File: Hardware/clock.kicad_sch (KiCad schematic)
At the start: 7 parts, among them U6 SI53365, X1 ASV-24.576MHz-EJ-T

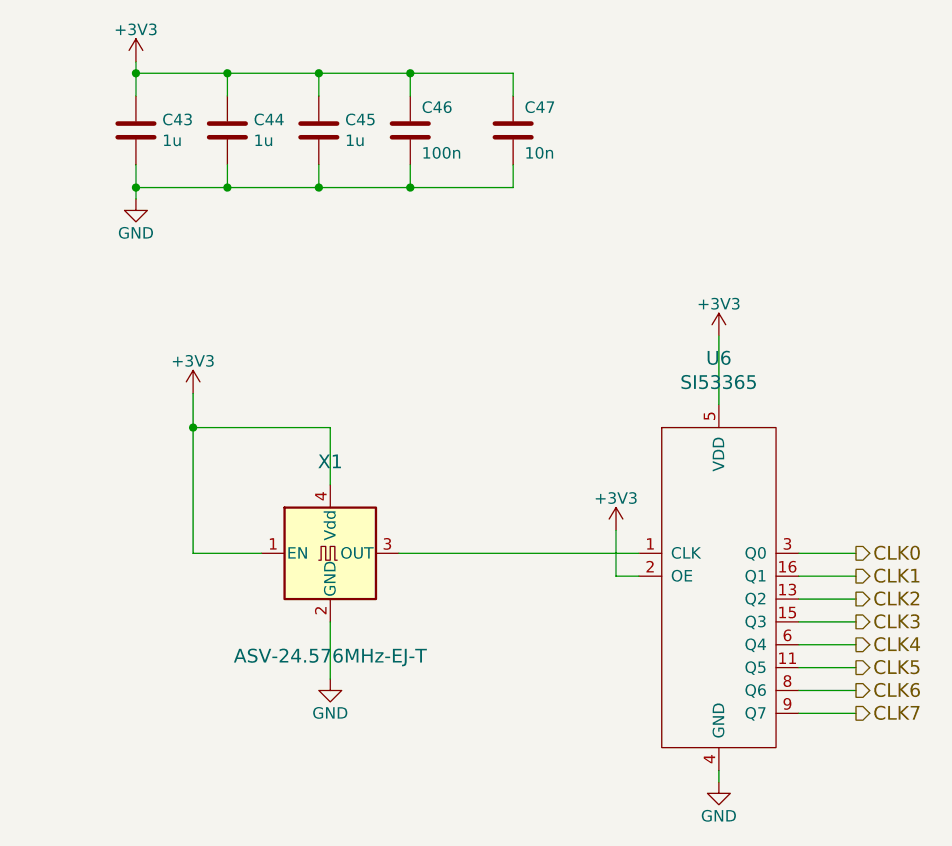
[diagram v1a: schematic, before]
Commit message: Updated clock buffer
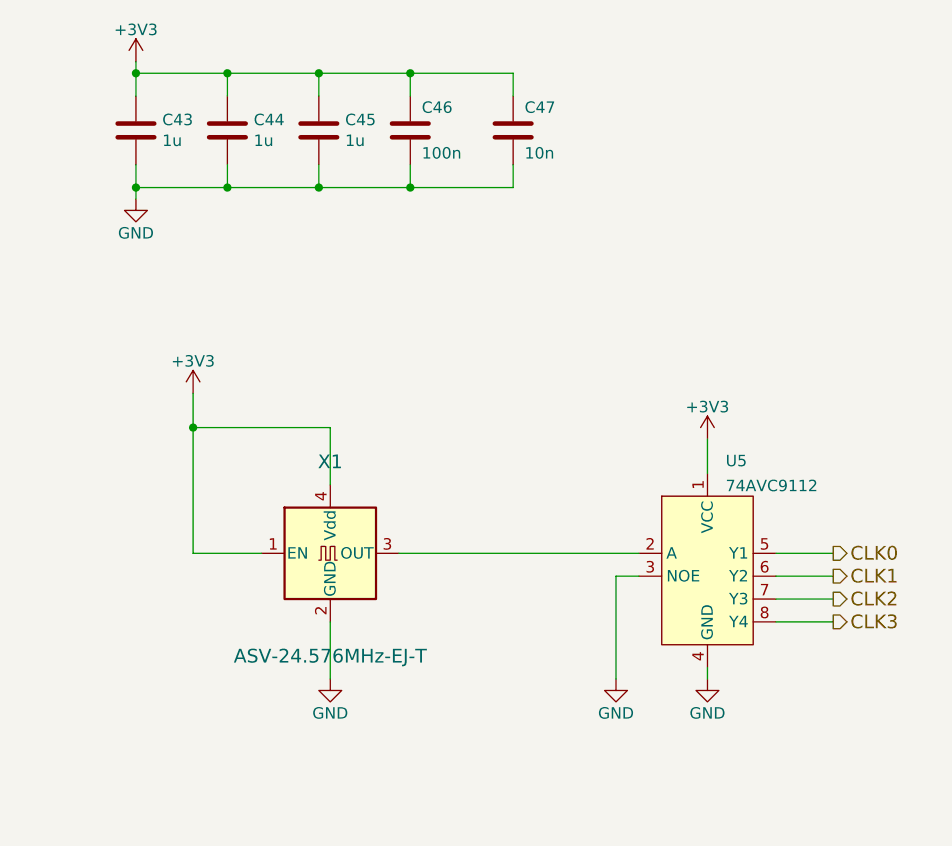
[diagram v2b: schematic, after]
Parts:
- removed U6: SI53365, Package_SO:TSSOP-16_4.4x5mm_P0.65mm, symbol buffers:SI53365
- added U5: 74AVC9112, buffers:NXP_XSON-8, symbol buffers:74AVC9112
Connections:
- net +3V3: now also U5.1 (VCC)
- net CLK0: now also U5.5 (Y1)
- net CLK1: now also U5.6 (Y2)
- net CLK2: now also U5.7 (Y3)
- net CLK3: now also U5.8 (Y4)
- net GND: now also U5.3 (NOE), U5.4 (GND)
- net at X1.3 (OUT): now also U5.2 (A)

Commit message: feat: updated amplifier IC, finalized design
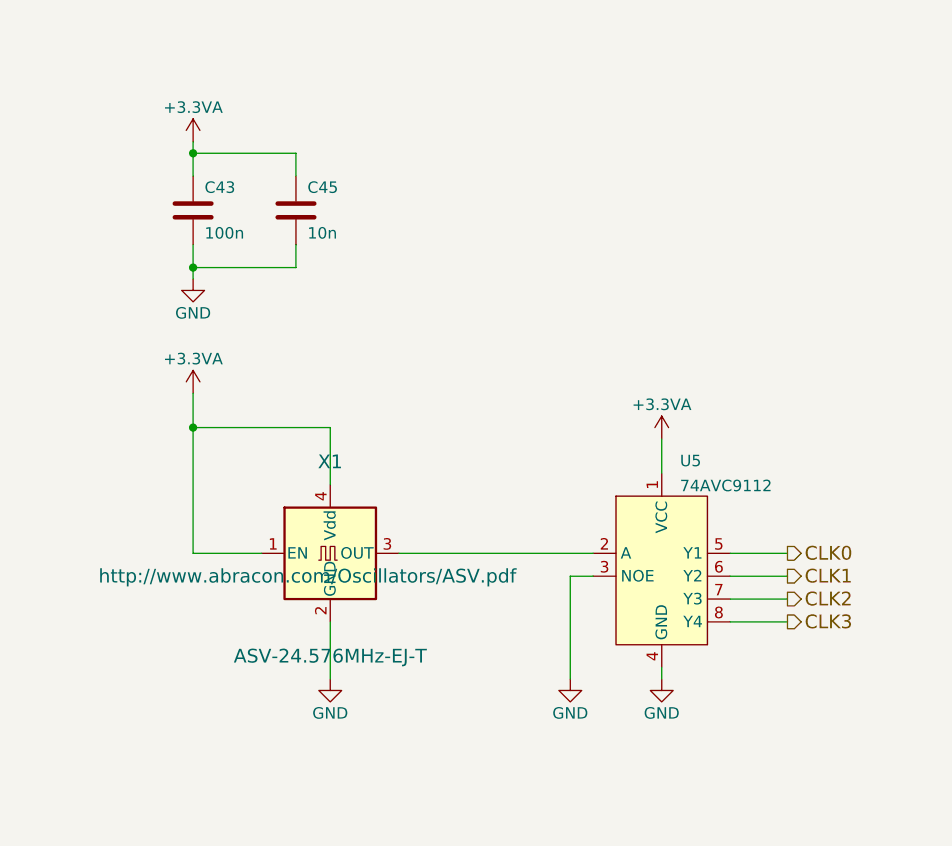
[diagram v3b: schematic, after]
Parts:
- removed C44: 1u, Capacitor_SMD:C_0805_2012Metric_Pad1.18x1.45mm_HandSolder, symbol Device:C
- removed C46: 100n, Capacitor_SMD:C_0603_1608Metric_Pad1.08x0.95mm_HandSolder, symbol Device:C
- removed C47: 10n, Capacitor_SMD:C_0603_1608Metric_Pad1.08x0.95mm_HandSolder, symbol Device:C
- C43: value 1u -> 100n; footprint Capacitor_SMD:C_0805_2012Metric_Pad1.18x1.45mm_HandSolder -> Capacitor_SMD:C_0402_1005Metric; Mfr.Nr. (none) -> GRM31CR71H475KA12L
- C45: value 1u -> 10n; footprint Capacitor_SMD:C_0805_2012Metric_Pad1.18x1.45mm_HandSolder -> Capacitor_SMD:C_0402_1005Metric; Mfr.Nr. (none) -> GRM31CR71H475KA12L
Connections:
- net +3V3 renamed +3.3VA
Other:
- moved on the sheet: U5

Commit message: prod. version blus mini a
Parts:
- C94: renamed from C45; MPN (none) -> C15195; Mfr.Nr. GRM31CR71H475KA12L -> (none)
- C96: renamed from C43; MPN (none) -> C307331; Mfr.Nr. GRM31CR71H475KA12L -> (none)
- U12: renamed from U5; footprint buffers:NXP_XSON-8 -> Package_SO:VSSOP-8_2.4x2.1mm_P0.5mm
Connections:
- net +3.3VA renamed +3.3V
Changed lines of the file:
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@@
       (effects (font (size 1.524 1.524)))
+    )
+    (property "Mfr.Nr." "" (id 4) (at 132.08 81.28 0)
+      (effects (font (size 1.27 1.27)) hide)
     )
     (pin "1")
@@
   (symbol (lib_id "power:GND") (at 168.91 95.25 0) (unit 1)
     (in_bom yes) (on_board yes)
-    (property "Reference" "#PWR062" (id 0) (at 168.91 101.6 0)
+    (property "Reference" "#PWR0132" (id 0) (at 168.91 101.6 0)
       (effects (font (size 1.27 1.27)) hide)
     )
     (property "Value" "GND" (id 1) (at 168.91 99.06 0))
     (property "Footprint" "" (id 2) (at 168.91 95.25 0)
-      (effects (font (size 1.524 1.524)))
+      (effects (font (size 1.27 1.27)) hide)
     )
     (property "Datasheet" "" (id 3) (at 168.91 95.25 0)
-      (effects (font (size 1.524 1.524)))
+      (effects (font (size 1.27 1.27)) hide)
     )
     (pin "1")
@@
   (symbol (lib_id "power:GND") (at 132.08 95.25 0) (unit 1)
     (in_bom yes) (on_board yes)
-    (property "Reference" "#PWR059" (id 0) (at 132.08 101.6 0)
+    (property "Reference" "#PWR0135" (id 0) (at 132.08 101.6 0)
       (effects (font (size 1.27 1.27)) hide)
     )
     (property "Value" "GND" (id 1) (at 132.08 99.06 0))
     (property "Footprint" "" (id 2) (at 132.08 95.25 0)
-      (effects (font (size 1.524 1.524)))
+      (effects (font (size 1.27 1.27)) hide)
     )
     (property "Datasheet" "" (id 3) (at 132.08 95.25 0)
-      (effects (font (size 1.524 1.524)))
+      (effects (font (size 1.27 1.27)) hide)
     )
     (pin "1")
@@
   (symbol (lib_id "power:GND") (at 116.84 50.8 0) (unit 1)
     (in_bom yes) (on_board yes)
-    (property "Reference" "#PWR057" (id 0) (at 116.84 57.15 0)
+    (property "Reference" "#PWR0130" (id 0) (at 116.84 57.15 0)
       (effects (font (size 1.27 1.27)) hide)
     )
     (property "Value" "GND" (id 1) (at 116.84 54.61 0))
     (property "Footprint" "" (id 2) (at 116.84 50.8 0)
-      (effects (font (size 1.524 1.524)))
+      (effects (font (size 1.27 1.27)) hide)
     )
     (property "Datasheet" "" (id 3) (at 116.84 50.8 0)
-      (effects (font (size 1.524 1.524)))
+      (effects (font (size 1.27 1.27)) hide)
     )
     (pin "1")
   )
-  (symbol (lib_id "power:+3.3VA") (at 116.84 63.5 0) (unit 1)
+  (symbol (lib_id "power:+3.3V") (at 116.84 63.5 0) (unit 1)
     (in_bom yes) (on_board yes)
-    (property "Reference" "#PWR0148" (id 0) (at 116.84 67.31 0)
+    (property "Reference" "#PWR0112" (id 0) (at 116.84 67.31 0)
       (effects (font (size 1.27 1.27)) hide)
     )
-    (property "Value" "+3.3VA" (id 1) (at 116.84 59.69 0))
+    (property "Value" "+3.3V" (id 1) (at 116.84 59.944 0))
     (property "Footprint" "" (id 2) (at 116.84 63.5 0)
       (effects (font (size 1.27 1.27)) hide)
@@
   (symbol (lib_id "Device:C") (at 128.27 43.18 0) (unit 1)
     (in_bom yes) (on_board yes)
-    (property "Reference" "C45" (id 0) (at 129.54 40.64 0)
+    (property "Reference" "C94" (id 0) (at 129.54 40.64 0)
       (effects (font (size 1.27 1.27)) (justify left))
     )
@@
       (effects (font (size 1.27 1.27)) hide)
     )
-    (property "Mfr.Nr." "GRM31CR71H475KA12L" (id 4) (at 128.27 43.18 0)
+    (property "Mfr.Nr." "" (id 4) (at 128.27 43.18 0)
       (effects (font (size 1.524 1.524)) hide)
+    )
+    (property "MPN" "C15195" (id 5) (at 128.27 43.18 0)
+      (effects (font (size 1.27 1.27)) hide)
     )
     (pin "1")
@@
   (symbol (lib_id "power:GND") (at 158.75 95.25 0) (unit 1)
     (in_bom yes) (on_board yes)
-    (property "Reference" "#PWR0128" (id 0) (at 158.75 101.6 0)
+    (property "Reference" "#PWR0134" (id 0) (at 158.75 101.6 0)
       (effects (font (size 1.27 1.27)) hide)
     )
     (property "Value" "GND" (id 1) (at 158.75 99.06 0))
     (property "Footprint" "" (id 2) (at 158.75 95.25 0)
-      (effects (font (size 1.524 1.524)))
+      (effects (font (size 1.27 1.27)) hide)
     )
     (property "Datasheet" "" (id 3) (at 158.75 95.25 0)
-      (effects (font (size 1.524 1.524)))
+      (effects (font (size 1.27 1.27)) hide)
     )
     (pin "1")
@@
   (symbol (lib_id "Device:C") (at 116.84 43.18 0) (unit 1)
     (in_bom yes) (on_board yes)
-    (property "Reference" "C43" (id 0) (at 118.11 40.64 0)
+    (property "Reference" "C96" (id 0) (at 118.11 40.64 0)
       (effects (font (size 1.27 1.27)) (justify left))
     )
@@
       (effects (font (size 1.27 1.27)) hide)
     )
-    (property "Mfr.Nr." "GRM31CR71H475KA12L" (id 4) (at 116.84 43.18 0)
+    (property "Mfr.Nr." "" (id 4) (at 116.84 43.18 0)
       (effects (font (size 1.524 1.524)) hide)
+    )
+    (property "MPN" "C307331" (id 5) (at 116.84 43.18 0)
+      (effects (font (size 1.27 1.27)) hide)
     )
     (pin "1")
@@
   (symbol (lib_id "buffers:74AVC9112") (at 167.64 74.93 0) (unit 1)
     (in_bom yes) (on_board yes) (fields_autoplaced)
-    (property "Reference" "U5" (id 0) (at 170.9294 71.0143 0)
+    (property "Reference" "U12" (id 0) (at 170.9294 71.0143 0)
       (effects (font (size 1.27 1.27)) (justify left))
     )
@@
       (effects (font (size 1.27 1.27)) (justify left))
     )
-    (property "Footprint" "buffers:NXP_XSON-8" (id 2) (at 167.64 74.93 0)
+    (property "Footprint" "Package_SO:VSSOP-8_2.4x2.1mm_P0.5mm" (id 2) (at 167.64 74.93 0)
       (effects (font (size 1.27 1.27)) hide)
     )
     (property "Datasheet" "" (id 3) (at 167.64 74.93 0)
+      (effects (font (size 1.27 1.27)) hide)
+    )
+    (property "Mfr.Nr." "" (id 4) (at 167.64 74.93 0)
       (effects (font (size 1.27 1.27)) hide)
     )
@@
     (pin "8")
   )
-  (symbol (lib_id "power:+3.3VA") (at 168.91 68.58 0) (unit 1)
+  (symbol (lib_id "power:+3.3V") (at 168.91 68.58 0) (unit 1)
     (in_bom yes) (on_board yes)
-    (property "Reference" "#PWR0146" (id 0) (at 168.91 72.39 0)
+    (property "Reference" "#PWR0131" (id 0) (at 168.91 72.39 0)
       (effects (font (size 1.27 1.27)) hide)
     )
-    (property "Value" "+3.3VA" (id 1) (at 168.91 64.77 0))
+    (property "Value" "+3.3V" (id 1) (at 168.91 65.024 0))
     (property "Footprint" "" (id 2) (at 168.91 68.58 0)
       (effects (font (size 1.27 1.27)) hide)
@@
     (pin "1")
   )
-  (symbol (lib_id "power:+3.3VA") (at 116.84 35.56 0) (unit 1)
+  (symbol (lib_id "power:+3.3V") (at 116.84 35.56 0) (unit 1)
     (in_bom yes) (on_board yes)
-    (property "Reference" "#PWR0147" (id 0) (at 116.84 39.37 0)
+    (property "Reference" "#PWR0133" (id 0) (at 116.84 39.37 0)
       (effects (font (size 1.27 1.27)) hide)
     )
-    (property "Value" "+3.3VA" (id 1) (at 116.84 31.75 0))
+    (property "Value" "+3.3V" (id 1) (at 116.84 32.004 0))
     (property "Footprint" "" (id 2) (at 116.84 35.56 0)
       (effects (font (size 1.27 1.27)) hide)
